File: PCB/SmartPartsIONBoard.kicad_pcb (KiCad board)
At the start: 2 copper layers, 18.9 x 46.4 mm, 25 parts, among them J1 Conn_01x04, Q1 FDN337N, SW1 SW_Push, U1 MIC5205-2.5YM5, U2 MAX313CPE, U4 Logo-c, U5 ATmega328P-MU

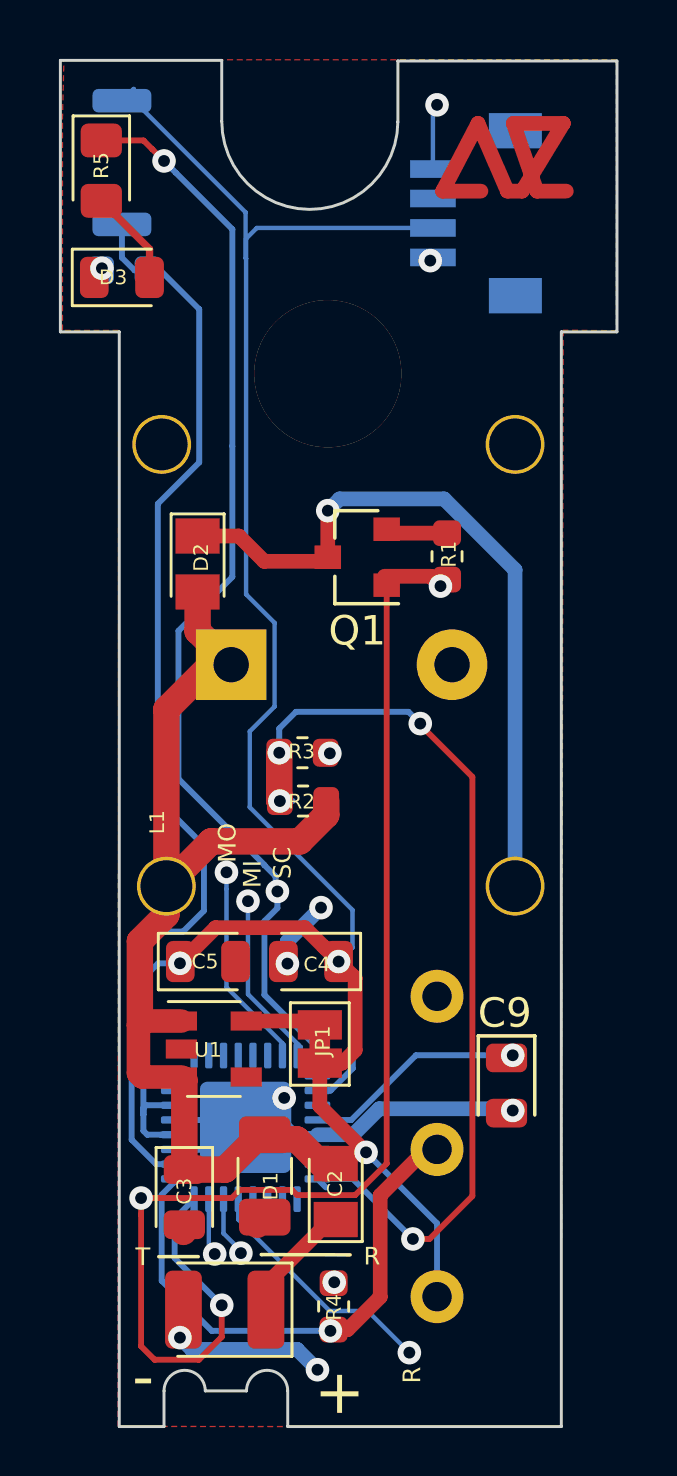
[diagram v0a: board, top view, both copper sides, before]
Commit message: GND Fix
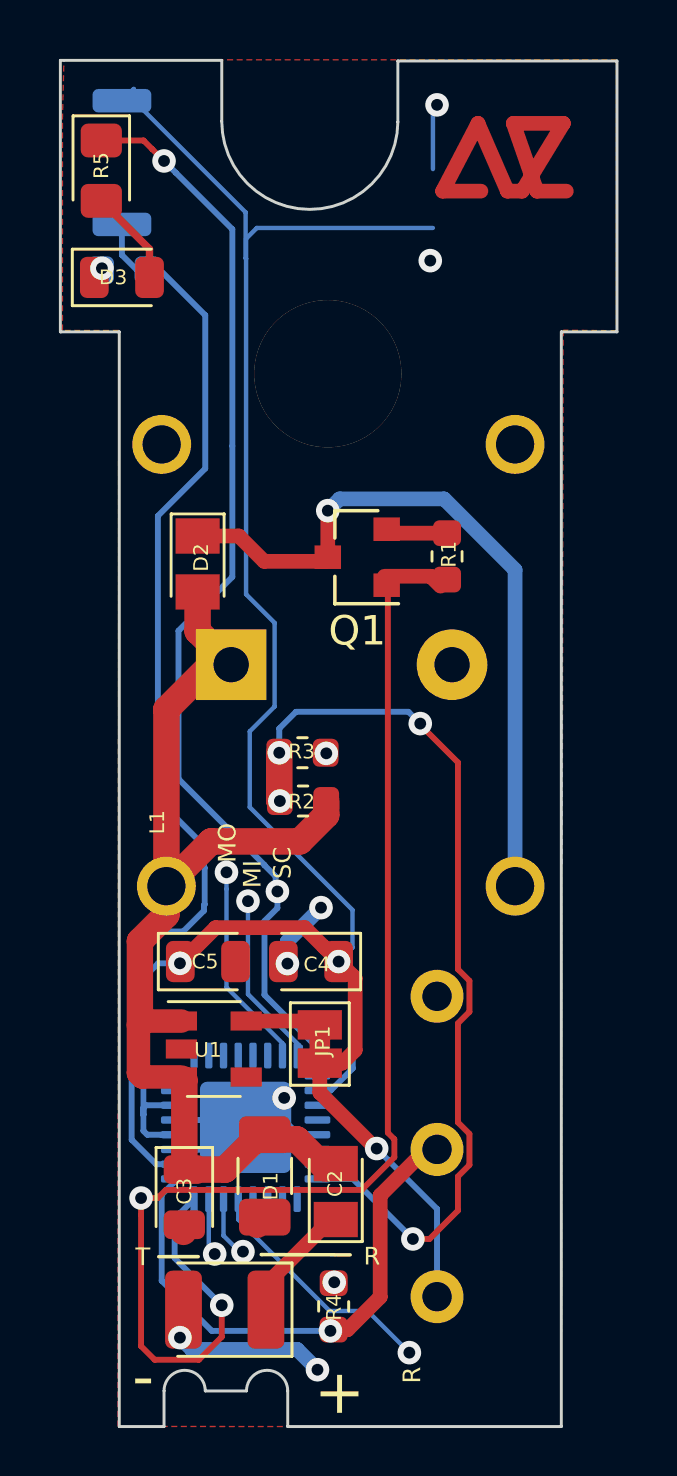
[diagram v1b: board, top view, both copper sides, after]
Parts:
- removed C9: 0.1u, LED_SMD:LED_0805_2012Metric
- removed J1: Conn_01x04, Ae_Logo:jst_4_smd
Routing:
- net Net-(C9-Pad1): track 7.54 -> 0.00 mm, vias 1 -> 0
- net GND: track 34.8 -> 27.8 mm, vias 11 -> 10
- net A1: track 32.0 -> 31.4 mm
- net D2: track 44.7 -> 44.8 mm, vias 3 -> 2
- added copper zone on F.Cu, net GND
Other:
- net class Default: clearance 0.2 -> 0.1
- rule trace_clearance: 0.2 -> 0.1

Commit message: Eye And Oled Display
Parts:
- added Brd1: SSD1306, ssd1306:128x64OLED, F.Cu at (114.3, 55.6)
- added D4: LED_Small, LED_THT:LED_D3.0mm_Horizontal_O1.27mm_Z2.0mm_IRBlack, F.Cu at (98.3, 24.2)
- added J1: Conn_01x04, Ae_Logo:jst_4_smd, F.Cu at (75.9, 36.9)
- added J2: Conn_01x04, Ae_Logo:jst_4_smd, F.Cu at (110.6, 35.1)
- added Q2: Q_Photo_NPN, LED_THT:LED_D3.0mm_Horizontal_O1.27mm_Z2.0mm_Clear, F.Cu at (126.7, 21.9)
- added R8: 100R, Resistor_SMD:R_0603_1608Metric, F.Cu at (111.5, 29.2)
- added R9: 10K, Resistor_SMD:R_0603_1608Metric, F.Cu at (113.6, 29.2)
- moved U4 12.3 mm to (66.6, 21.8)
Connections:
- U5 pad 23: A0 -> (no net)
- U5 pad 27: (no net) -> A4
- U5 pad 28: (no net) -> A5
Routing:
- net VCC: track 76.3 -> 70.3 mm
- net GND: track 27.8 -> 25.6 mm

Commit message: fix
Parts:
- added C8: 0.1u, LED_SMD:LED_0603_1608Metric, F.Cu at (129.5, 69.8)
- added C9: 0.1u, LED_SMD:LED_0805_2012Metric, F.Cu at (124.0, 75.8)
- added R10: R_Small_US, Resistor_SMD:R_0603_1608Metric, F.Cu at (128.2, 75.5)
- added R11: R_Small_US, Resistor_SMD:R_0603_1608Metric, F.Cu at (128.2, 78.0)
- added R7: 10k, LED_SMD:LED_0603_1608Metric, F.Cu at (129.5, 72.4)
- added SW2: SW_Push, Button_Switch_SMD:SW_Push_SPST_NO_Alps_SKRK, F.Cu at (118.5, 70.8)
- added SW3: SW_Push, Button_Switch_SMD:SW_Push_SPST_NO_Alps_SKRK, F.Cu at (118.5, 75.2)
- moved U4 75.4 mm to (125.2, 69.3)
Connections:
- U5 pad 11: DTR -> (no net)
- U5 pad 15: MOSI -> (no net)
- U5 pad 16: MISO -> (no net)
- U5 pad 30: RXI -> (no net)
- U5 pad 31: TXO -> (no net)
- U5 pad 7: Net-(C7-Pad1) -> (no net)
- U5 pad 8: Net-(C6-Pad1) -> (no net)
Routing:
- net (no net): track 0.00 -> 17.1 mm, vias 0 -> 4
- net MOSI: track 7.01 -> 0.00 mm, vias 1 -> 0
- net MISO: track 6.04 -> 0.00 mm, vias 1 -> 0
- net RXI: track 2.08 -> 0.00 mm, vias 1 -> 0
- net TXO: track 1.95 -> 0.00 mm, vias 1 -> 0
